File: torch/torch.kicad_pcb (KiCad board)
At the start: 2 copper layers, 66 x 15.2 mm, 4 parts, among them SW1 SW_DPST_x2

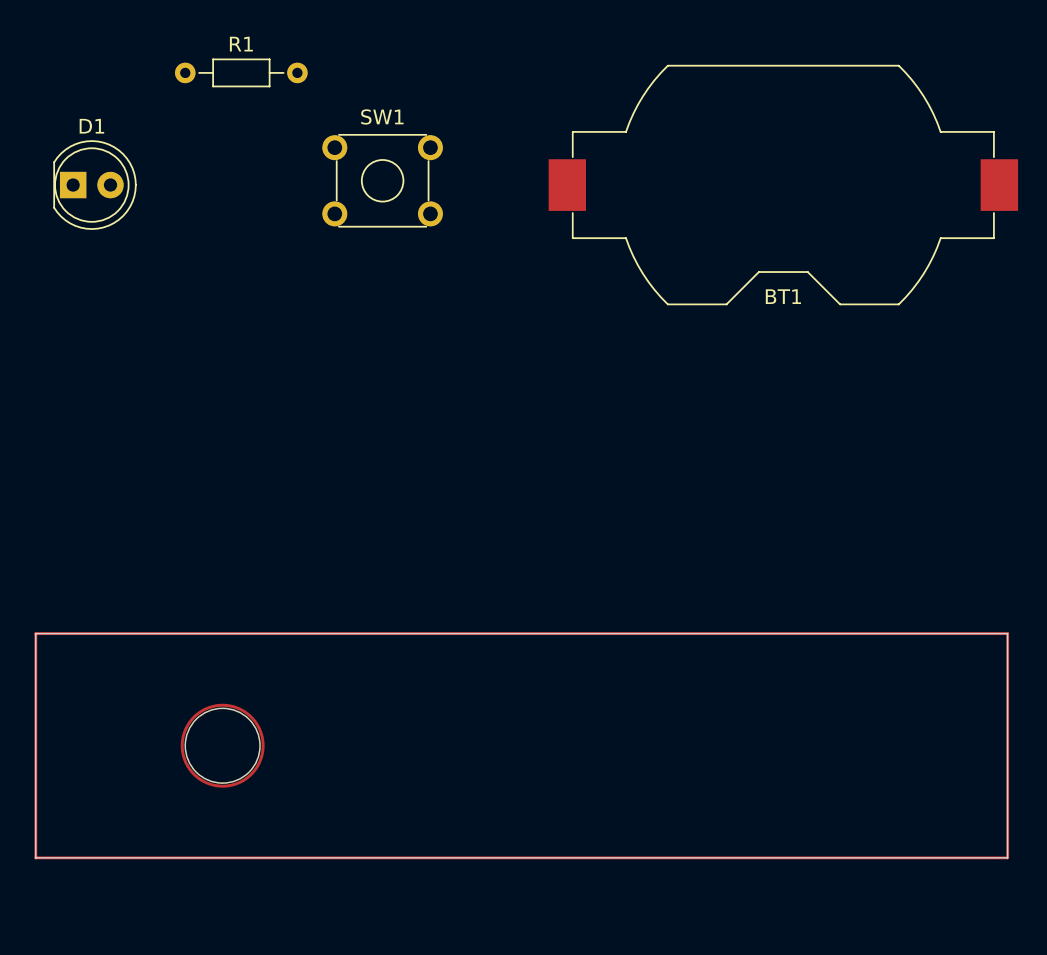
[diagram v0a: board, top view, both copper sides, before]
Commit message: feat: wire footprints
Signed-off-by: Matt Gleich <git@mattglei.ch>
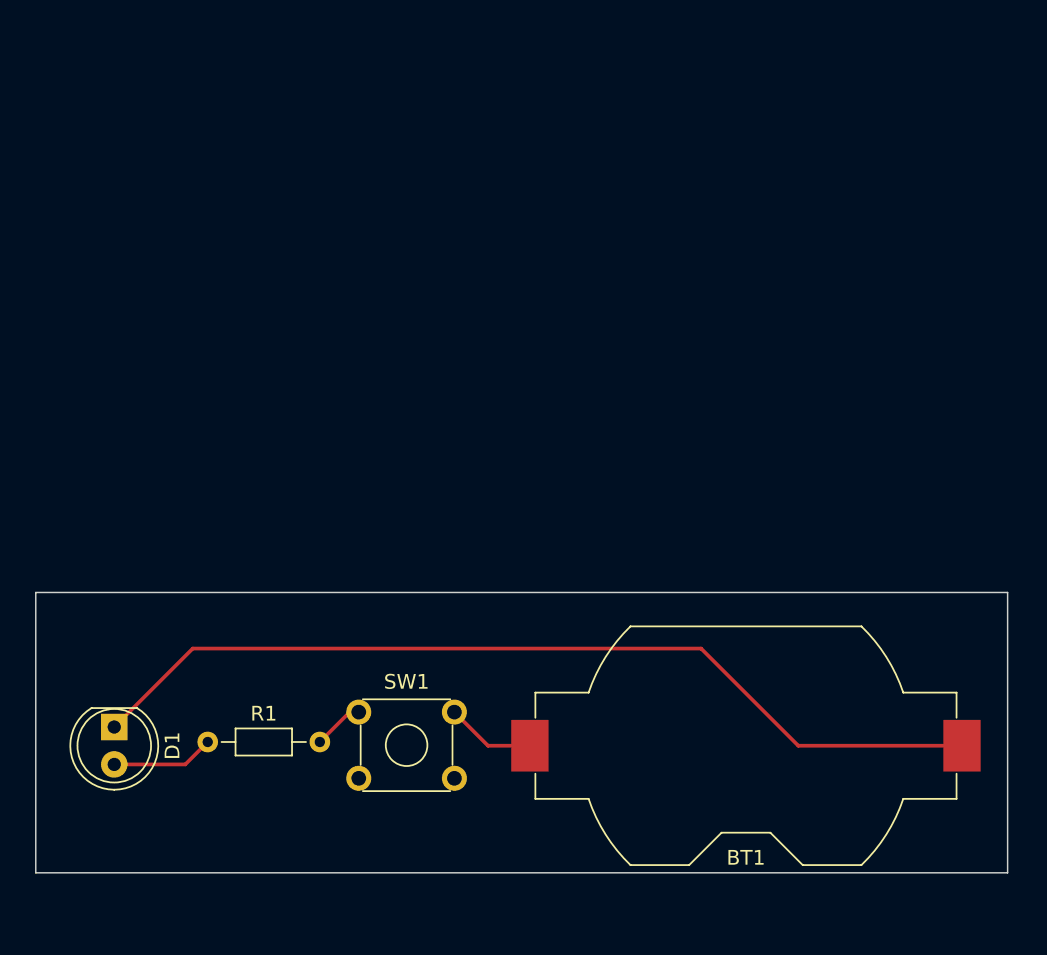
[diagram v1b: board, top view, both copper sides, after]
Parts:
- moved R1 45.5 mm to (131.1, 75.9)
- moved SW1 38.4 mm to (141.3, 73.9)
- moved BT1 38.2 mm to (167.6, 76.2)
- moved D1 36.9 mm to (124.7, 74.9), turned to -90 degrees
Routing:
- net /LED_cathode: track 0.00 -> 62.6 mm
- net /LED_anode: track 0.00 -> 6.98 mm
- net /bat_pos: track 0.00 -> 6.08 mm
- net Net-(R1-Pad2): track 0.00 -> 3.49 mm
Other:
- board size 66 x 15.2 mm -> 66 x 19 mm
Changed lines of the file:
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@@
   (net 4 "Net-(R1-Pad2)")
   (footprint "Resistor_THT:R_Axial_DIN0204_L3.6mm_D1.6mm_P7.62mm_Horizontal" (layer "F.Cu")
-    (at 129.54 30.48)
+    (at 131.064 75.946)
     (descr "Resistor, Axial_DIN0204 series, Axial, Horizontal, pin pitch=7.62mm, 0.167W, length*diameter=3.6*1.6mm^2, http://cdn-reichelt.de/documents/datenblatt/B400/1_4W%23YAG.pdf")
     (tags "Resistor Axial_DIN0204 series Axial Horizontal pin pitch 7.62mm 0.167W length 3.6mm diameter 1.6mm")
@@
   )
   (footprint "Button_Switch_THT:SW_TH_Tactile_Omron_B3F-10xx" (layer "F.Cu")
-    (at 139.7 35.56)
+    (at 141.328 73.914)
     (descr "SW_TH_Tactile_Omron_B3F-10xx_https://www.omron.com/ecb/products/pdf/en-b3f.pdf")
     (tags "Omron B3F-10xx")
@@
   )
   (footprint "Battery:BatteryHolder_Keystone_1058_1x2032" (layer "F.Cu")
-    (at 170.18 38.1)
+    (at 167.64 76.2)
     (descr "http://www.keyelco.com/product-pdf.cfm?p=14028")
     (tags "Keystone type 1058 coin cell retainer")
@@
   )
   (footprint "LED_THT:LED_D5.0mm" (layer "F.Cu")
-    (at 121.92 38.1)
+    (at 124.714 74.93 -90)
     (descr "LED, diameter 5.0mm, 2 pins, http://cdn-reichelt.de/documents/datenblatt/A500/LL-504BC2E-009.pdf")
     (tags "LED diameter 5.0mm 2 pins")
@@
     (property "Sheetname" "")
     (attr through_hole)
-    (fp_text reference "D1" (at 1.27 -3.96) (layer "F.SilkS")
-      (effects (font (size 1 1) (thickness 0.15)))
-    )
-    (fp_text value "LED" (at 1.27 3.96) (layer "F.Fab")
-      (effects (font (size 1 1) (thickness 0.15)))
-    )
-    (fp_text user "${REFERENCE}" (at 1.25 0) (layer "F.Fab")
+    (fp_text reference "D1" (at 1.27 -3.96 90) (layer "F.SilkS")
+      (effects (font (size 1 1) (thickness 0.15)))
+    )
+    (fp_text value "LED" (at 1.27 3.96 90) (layer "F.Fab")
+      (effects (font (size 1 1) (thickness 0.15)))
+    )
+    (fp_text user "${REFERENCE}" (at 1.25 0 90) (layer "F.Fab")
       (effects (font (size 0.8 0.8) (thickness 0.2)))
     )
@@
     (fp_arc (start -1.23 -1.469694) (mid 4.17 0.000016) (end -1.230016 1.469666) (layer "F.Fab") (width 0.1))
     (fp_circle (center 1.27 0) (end 3.77 0) (layer "F.Fab") (width 0.1) (fill none))
-    (pad "1" thru_hole rect (at 0 0) (size 1.8 1.8) (drill 0.9) (layers *.Cu *.Mask)
+    (pad "1" thru_hole rect (at 0 0 270) (size 1.8 1.8) (drill 0.9) (layers *.Cu *.Mask)
       (net 2 "/LED_cathode") (pinfunction "K") (pintype "passive"))
-    (pad "2" thru_hole circle (at 2.54 0) (size 1.8 1.8) (drill 0.9) (layers *.Cu *.Mask)
+    (pad "2" thru_hole circle (at 2.54 0 270) (size 1.8 1.8) (drill 0.9) (layers *.Cu *.Mask)
       (net 3 "/LED_anode") (pinfunction "A") (pintype "passive"))
     (model "${KICAD6_3DMODEL_DIR}/LED_THT.3dshapes/LED_D5.0mm.wrl"
@@
     )
   )
-  (gr_circle (center 132.08 76.2) (end 133.132102 73.66) (layer "F.Cu") (width 0.2) (fill none))
-  (gr_rect (start 185.42 83.82) (end 119.38 68.58) (layer "F.Cu") (width 0.2) (fill none))
-  (gr_line (start 119.38 83.82) (end 185.42 83.82) (layer "Edge.Cuts") (width 0.1))
-  (gr_line (start 119.38 68.58) (end 119.38 83.82) (layer "Edge.Cuts") (width 0.1))
-  (gr_circle (center 132.08 76.2) (end 134.62 76.2) (layer "Edge.Cuts") (width 0.1) (fill none))
-  (gr_line (start 185.42 83.82) (end 185.42 68.58) (layer "Edge.Cuts") (width 0.1))
-  (gr_line (start 185.42 68.58) (end 119.38 68.58) (layer "Edge.Cuts") (width 0.1))
+  (gr_line (start 119.38 84.836) (end 185.42 84.836) (layer "Edge.Cuts") (width 0.1))
+  (gr_line (start 119.38 65.786) (end 119.38 84.836) (layer "Edge.Cuts") (width 0.1))
+  (gr_line (start 185.42 84.836) (end 185.42 65.786) (layer "Edge.Cuts") (width 0.1))
+  (gr_line (start 185.42 65.786) (end 119.38 65.786) (layer "Edge.Cuts") (width 0.1))
+  (gr_rect (start 185.42 84.836) (end 119.38 65.786) (layer "User.1") (width 0.2) (fill none))
+  (segment (start 150.114 76.2) (end 152.96 76.2) (width 0.25) (layer "F.Cu") (net 1))
+  (segment (start 147.828 73.914) (end 150.114 76.2) (width 0.25) (layer "F.Cu") (net 1))
+  (segment (start 130.048 69.596) (end 164.592 69.596) (width 0.25) (layer "F.Cu") (net 2))
+  (segment (start 164.592 69.596) (end 171.196 76.2) (width 0.25) (layer "F.Cu") (net 2))
+  (segment (start 124.714 74.93) (end 130.048 69.596) (width 0.25) (layer "F.Cu") (net 2))
+  (segment (start 171.196 76.2) (end 182.32 76.2) (width 0.25) (layer "F.Cu") (net 2))
+  (segment (start 124.714 77.47) (end 129.54 77.47) (width 0.25) (layer "F.Cu") (net 3))
+  (segment (start 129.54 77.47) (end 131.064 75.946) (width 0.25) (layer "F.Cu") (net 3))
+  (segment (start 140.716 73.914) (end 141.328 73.914) (width 0.25) (layer "F.Cu") (net 4))
+  (segment (start 138.684 75.946) (end 140.716 73.914) (width 0.25) (layer "F.Cu") (net 4))
 )

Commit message: feat: add arcs
Signed-off-by: Matt Gleich <git@mattglei.ch>
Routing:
- net /LED_cathode: track 62.6 -> 60.4 mm
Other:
- board size 66 x 19 mm -> 66.4 x 24.3 mm
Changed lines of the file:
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@@
     )
   )
-  (gr_line (start 119.38 84.836) (end 185.42 84.836) (layer "Edge.Cuts") (width 0.1))
-  (gr_line (start 119.38 65.786) (end 119.38 84.836) (layer "Edge.Cuts") (width 0.1))
-  (gr_line (start 185.42 84.836) (end 185.42 65.786) (layer "Edge.Cuts") (width 0.1))
-  (gr_line (start 185.42 65.786) (end 119.38 65.786) (layer "Edge.Cuts") (width 0.1))
-  (gr_rect (start 185.42 84.836) (end 119.38 65.786) (layer "User.1") (width 0.2) (fill none))
+  (gr_line (start 184.531 81.788) (end 178.435 81.788) (layer "Edge.Cuts") (width 0.1))
+  (gr_line (start 124.714 81.788) (end 156.872217 81.788) (layer "Edge.Cuts") (width 0.1))
+  (gr_line (start 184.531 70.358) (end 178.308 70.358) (layer "Edge.Cuts") (width 0.1))
+  (gr_arc (start 185.42 80.899) (mid 185.159618 81.527618) (end 184.531 81.788) (layer "Edge.Cuts") (width 0.1))
+  (gr_line (start 185.42 80.899) (end 185.42 71.247) (layer "Edge.Cuts") (width 0.1))
+  (gr_arc (start 178.435 81.788) (mid 167.653608 88.347286) (end 156.872217 81.788) (layer "Edge.Cuts") (width 0.1))
+  (gr_arc (start 124.714 81.788) (mid 118.999 76.073) (end 124.714 70.358) (layer "Edge.Cuts") (width 0.1))
+  (gr_line (start 156.972 70.358) (end 124.714 70.358) (layer "Edge.Cuts") (width 0.1))
+  (gr_arc (start 156.972 70.358) (mid 167.64 64.037139) (end 178.308 70.358) (layer "Edge.Cuts") (width 0.1))
+  (gr_arc (start 184.531 70.358) (mid 185.159618 70.618382) (end 185.42 71.247) (layer "Edge.Cuts") (width 0.1))
+  (gr_rect (start 185.42 81.534) (end 119.38 68.58) (layer "User.1") (width 0.2) (fill none))
+  (gr_circle (center 167.64 76.2) (end 179.324 79.502) (layer "User.2") (width 0.15) (fill none))
   (segment (start 150.114 76.2) (end 152.96 76.2) (width 0.25) (layer "F.Cu") (net 1))
   (segment (start 147.828 73.914) (end 150.114 76.2) (width 0.25) (layer "F.Cu") (net 1))
-  (segment (start 130.048 69.596) (end 164.592 69.596) (width 0.25) (layer "F.Cu") (net 2))
-  (segment (start 164.592 69.596) (end 171.196 76.2) (width 0.25) (layer "F.Cu") (net 2))
-  (segment (start 124.714 74.93) (end 130.048 69.596) (width 0.25) (layer "F.Cu") (net 2))
   (segment (start 171.196 76.2) (end 182.32 76.2) (width 0.25) (layer "F.Cu") (net 2))
+  (segment (start 167.132 72.136) (end 171.196 76.2) (width 0.25) (layer "F.Cu") (net 2))
+  (segment (start 127.508 72.136) (end 167.132 72.136) (width 0.25) (layer "F.Cu") (net 2))
+  (segment (start 124.714 74.93) (end 127.508 72.136) (width 0.25) (layer "F.Cu") (net 2))
   (segment (start 124.714 77.47) (end 129.54 77.47) (width 0.25) (layer "F.Cu") (net 3))
   (segment (start 129.54 77.47) (end 131.064 75.946) (width 0.25) (layer "F.Cu") (net 3))

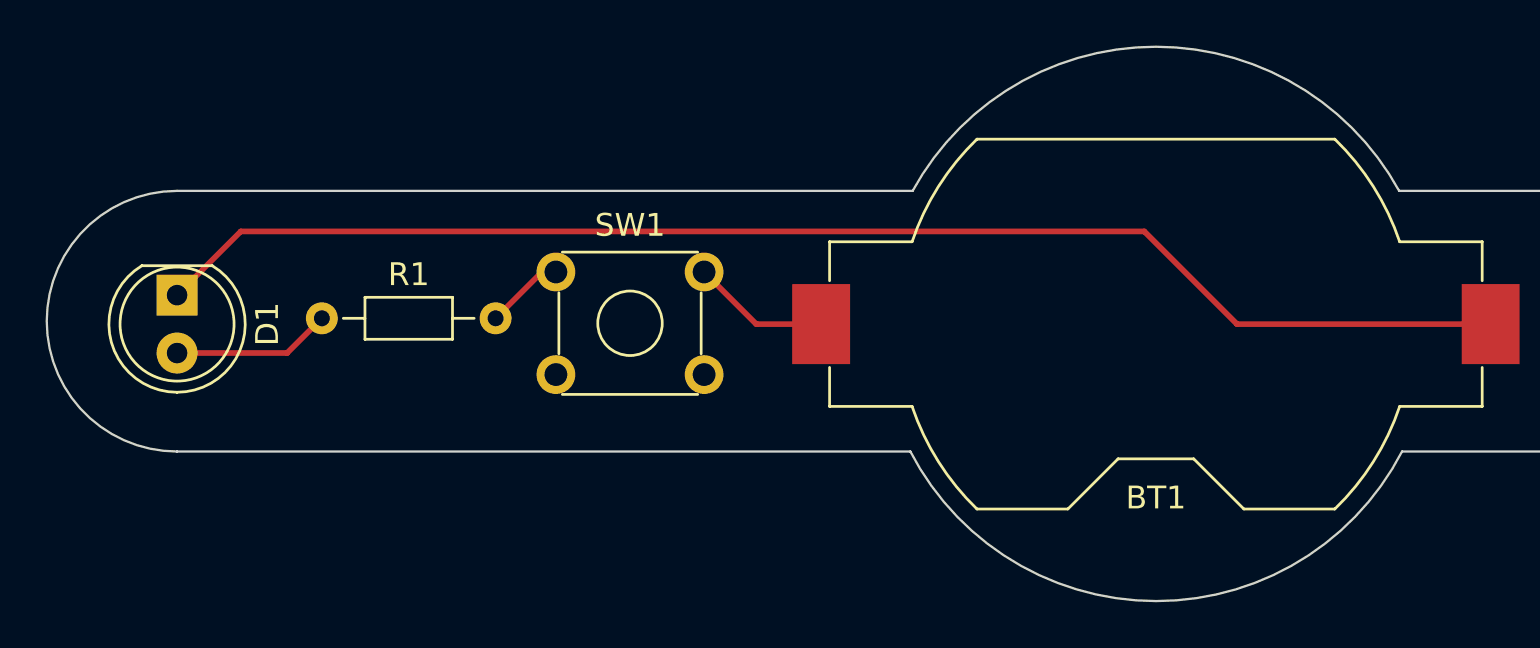
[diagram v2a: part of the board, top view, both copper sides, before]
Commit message: feat: silkscreen
Signed-off-by: Matt Gleich <git@mattglei.ch>
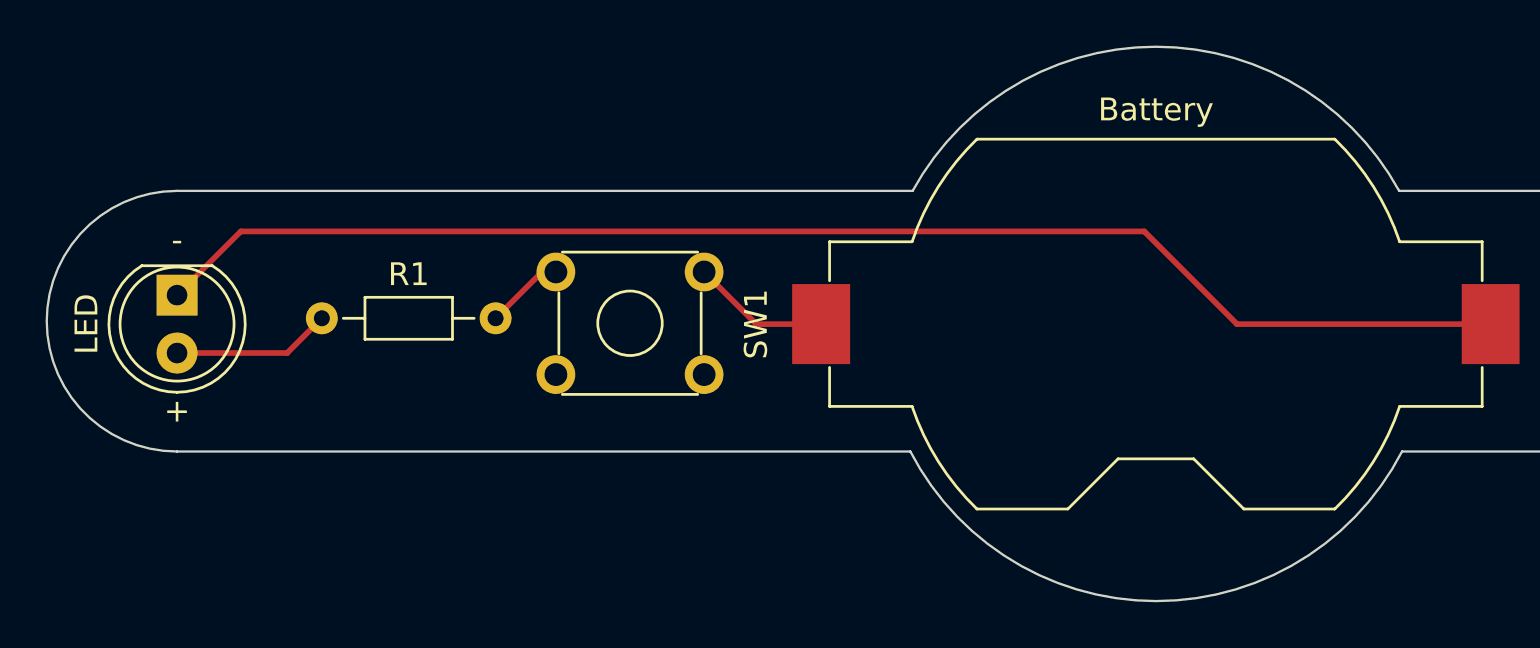
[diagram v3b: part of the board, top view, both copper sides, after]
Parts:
- added logo: LOGO, logo:logo, B.Cu at (167.6, 76.1)
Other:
- board text added: "+"
- board text added: "-"
- board text added: "github.com/gleich/pcbs"
- board text added: "© Matt Gleich 2022"
